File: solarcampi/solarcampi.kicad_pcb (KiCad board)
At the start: 2 copper layers, 65 x 30 mm, 6 parts, among them J1 Conn_02x20_Odd_Even

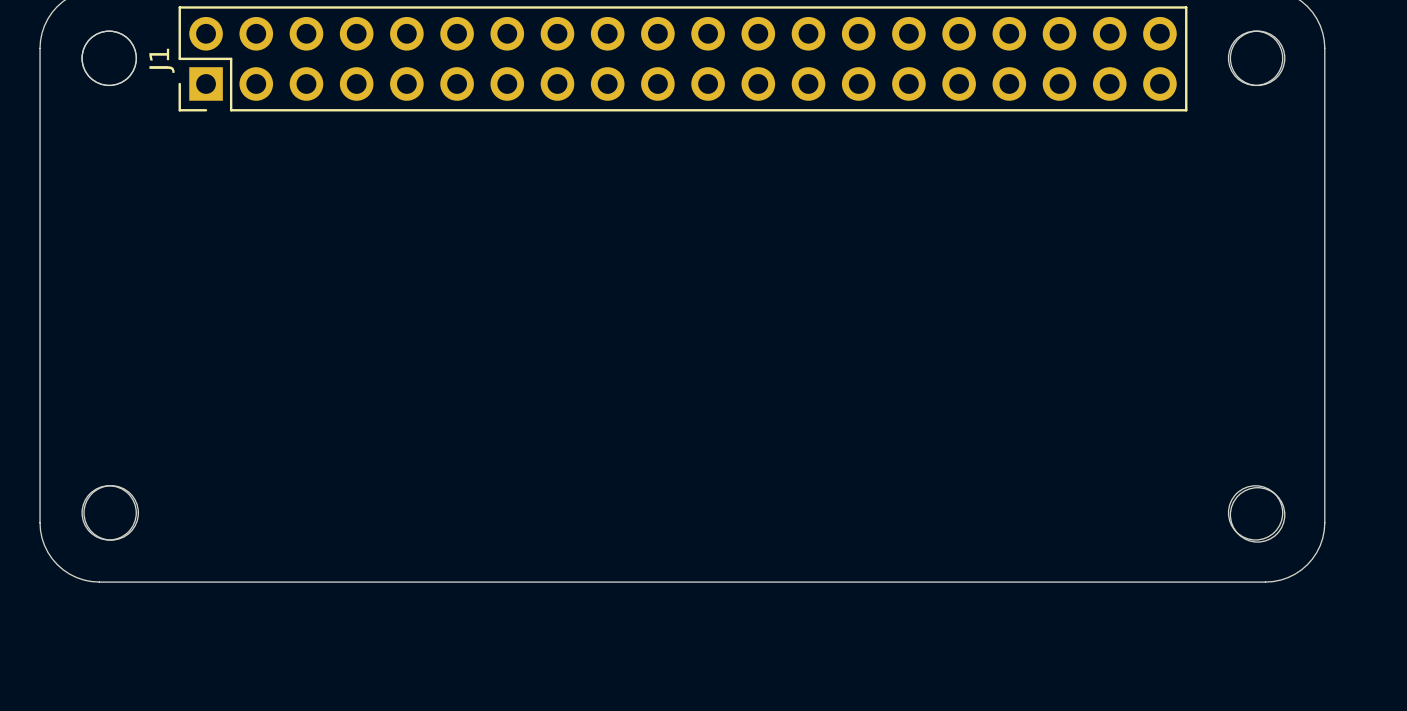
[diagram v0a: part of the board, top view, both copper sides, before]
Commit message: Add fuse, add decoupling caps, set footprints
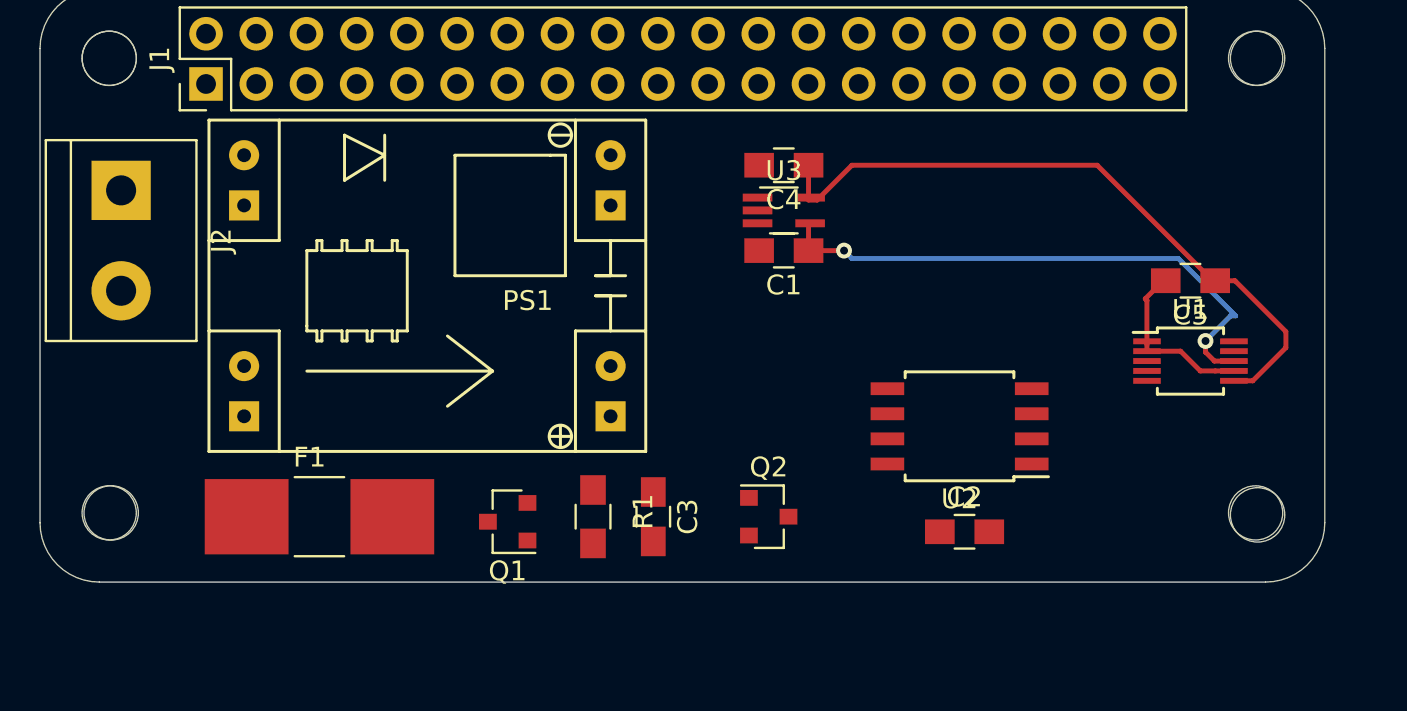
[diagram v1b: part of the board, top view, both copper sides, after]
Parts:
- added C1: 100n, Capacitors_SMD:C_0805_HandSoldering, F.Cu at (87.6, 62.2)
- added C2: 100n, Capacitors_SMD:C_0805_HandSoldering, F.Cu at (96.8, 76.5)
- added C3: 100n, Capacitors_SMD:C_0805_HandSoldering, F.Cu at (81.0, 75.7)
- added C4: 1µF, Capacitors_SMD:C_0805_HandSoldering, F.Cu at (87.6, 57.9)
- added C5: 100n, Capacitors_SMD:C_0805_HandSoldering, F.Cu at (108.2, 63.8)
- added F1: 1A, solarcampi:Fuse_SMD_HASF, F.Cu at (64.1, 75.7)
- added J2: Vin 12V, Connectors:bornier2, F.Cu at (54.1, 59.2)
- added PS1: MP1584EN, solarcampi:MP1584_buck_module, F.Cu at (69.6, 64.0)
- added Q1: IRLML 2244, TO_SOT_Packages_SMD:SOT-23, F.Cu at (73.7, 75.9)
- added Q2: BCR 108 SMD, TO_SOT_Packages_SMD:SOT-23, F.Cu at (86.9, 75.7)
- added R1: 10k, Resistors_SMD:R_0805_HandSoldering, F.Cu at (78.0, 75.7)
- added U1: INA226, Housings_SSOP:MSOP-10_3x3mm_Pitch0.5mm, F.Cu at (108.2, 67.8)
- added U2: ATtiny85-20SU, Housings_SOIC:SOIJ-8_5.3x5.3mm_Pitch1.27mm, F.Cu at (96.5, 71.1)
- added U3: TPS71533__SC70, TO_SOT_Packages_SMD:SOT-353_SC-70-5_Handsoldering, F.Cu at (87.6, 60.2)
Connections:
- J1 pad 6: Net-(J1-Pad6) -> GND
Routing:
- net +3V3: track 0.00 -> 34.3 mm
- net +12V: track 0.00 -> 28.6 mm, vias 0 -> 2
- net GND: track 0.00 -> 8.92 mm

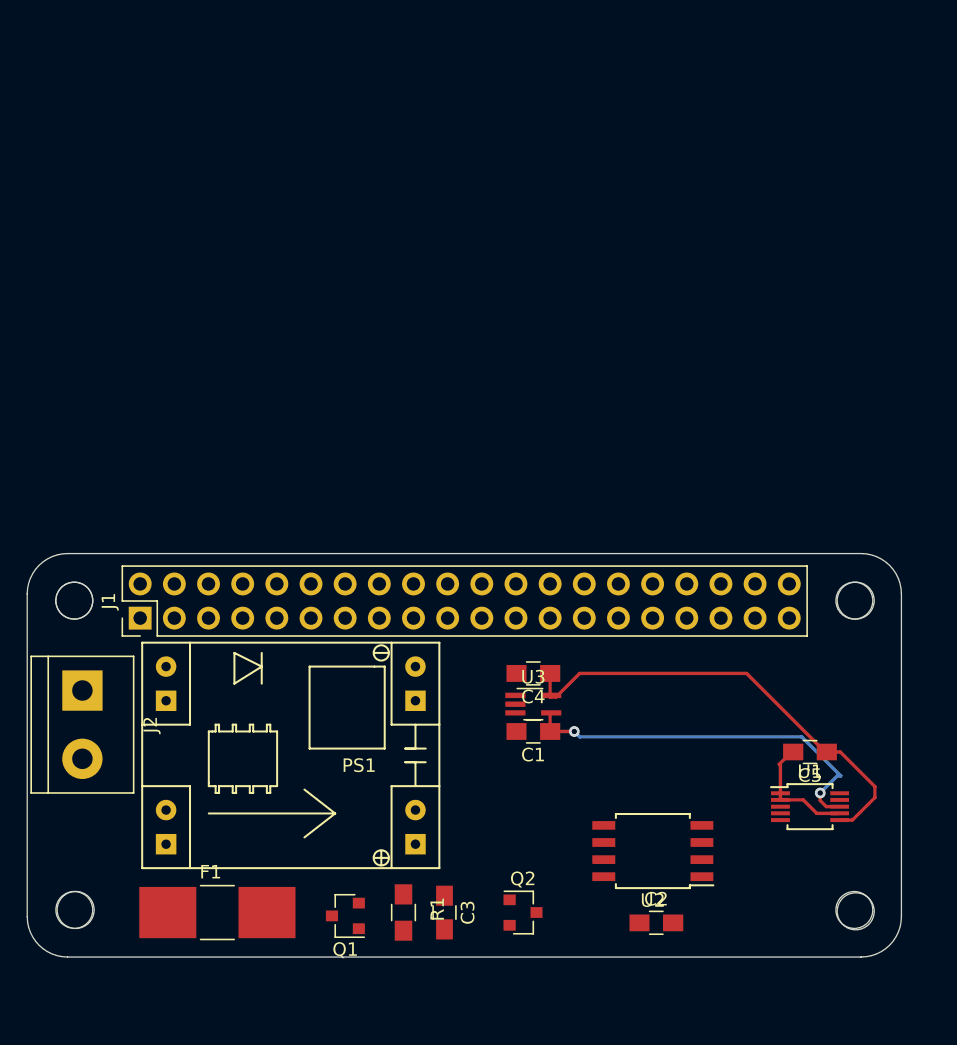
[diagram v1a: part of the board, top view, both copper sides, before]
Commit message: Add ISP header, FTDI header, more caps, power switching for INA and 2 I2C busses
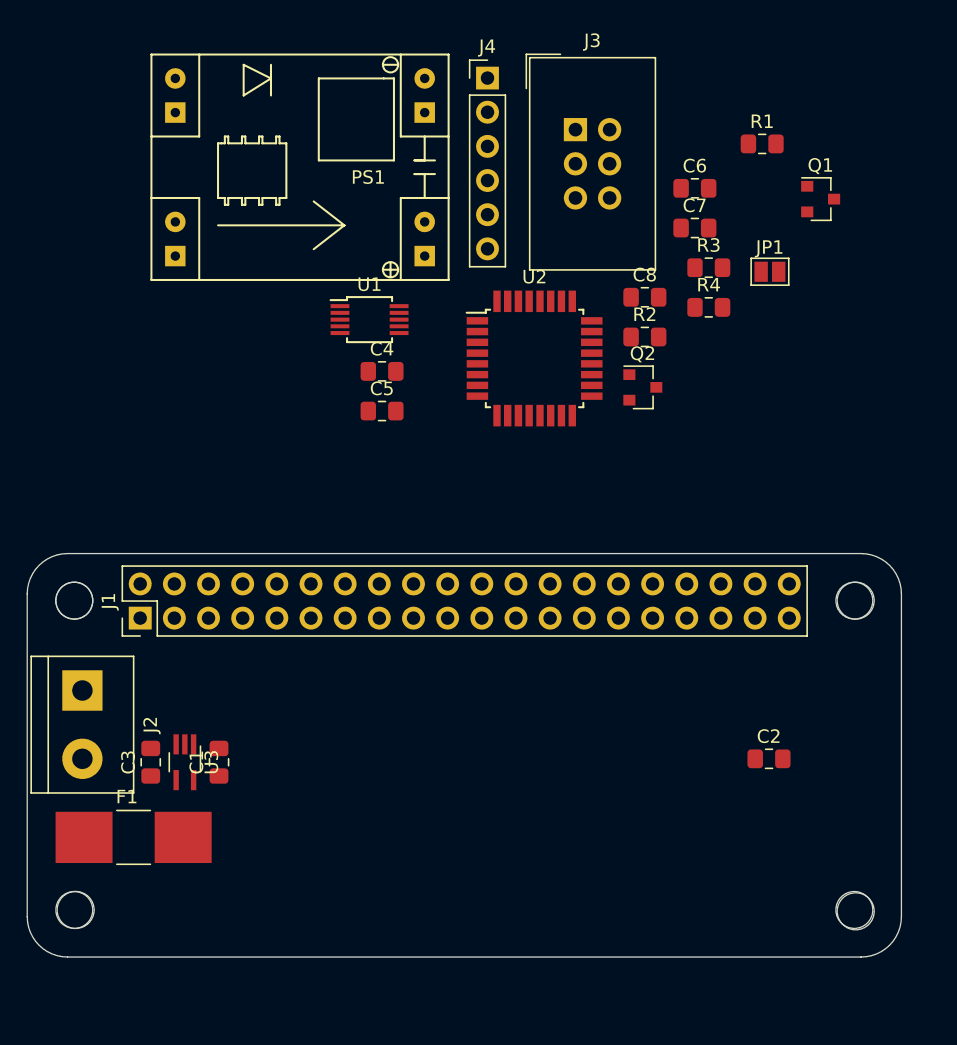
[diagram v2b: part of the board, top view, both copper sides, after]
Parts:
- added C6: 100n, Capacitor_SMD:C_0805_2012Metric_Pad1.15x1.40mm_HandSolder, F.Cu at (99.6, 21.8)
- added C7: 10µ, Capacitor_SMD:C_0805_2012Metric_Pad1.15x1.40mm_HandSolder, F.Cu at (99.6, 24.8)
- added C8: 10µ, Capacitor_SMD:C_0805_2012Metric_Pad1.15x1.40mm_HandSolder, F.Cu at (95.9, 29.9)
- added J3: AVR-ISP-6, Connector_IDC:IDC-Header_2x03_P2.54mm_Vertical, F.Cu at (90.8, 17.5)
- added J4: FTDI, Connector_PinHeader_2.54mm:PinHeader_1x06_P2.54mm_Vertical, F.Cu at (84.2, 13.6)
- added JP1: Jumper_2_Open, Jumper:SolderJumper-2_P1.3mm_Open_Pad1.0x1.5mm, F.Cu at (105.2, 28.0)
- added R2: 10k, Resistor_SMD:R_0805_2012Metric_Pad1.15x1.40mm_HandSolder, F.Cu at (95.9, 32.9)
- added R3: 4k7, Resistor_SMD:R_0805_2012Metric_Pad1.15x1.40mm_HandSolder, F.Cu at (100.7, 27.7)
- added R4: 4k7, Resistor_SMD:R_0805_2012Metric_Pad1.15x1.40mm_HandSolder, F.Cu at (100.7, 30.7)
- C1, C2, C3, C4, C5: footprint Capacitors_SMD:C_0805_HandSoldering -> Capacitor_SMD:C_0805_2012Metric_Pad1.15x1.40mm_HandSolder
- J2: footprint Connectors:bornier2 -> TerminalBlock:TerminalBlock_bornier-2_P5.08mm
- Q1, Q2: footprint TO_SOT_Packages_SMD:SOT-23 -> Package_TO_SOT_SMD:SOT-23
- R1: footprint Resistors_SMD:R_0805_HandSoldering -> Resistor_SMD:R_0805_2012Metric_Pad1.15x1.40mm_HandSolder
- U1: footprint Housings_SSOP:MSOP-10_3x3mm_Pitch0.5mm -> Package_SO:MSOP-10_3x3mm_P0.5mm
- U2: value ATtiny85-20SU -> ATmega328P-AU; footprint Housings_SOIC:SOIJ-8_5.3x5.3mm_Pitch1.27mm -> Package_QFP:TQFP-32_7x7mm_P0.8mm
- U3: footprint TO_SOT_Packages_SMD:SOT-353_SC-70-5_Handsoldering -> Package_TO_SOT_SMD:SOT-353_SC-70-5_Handsoldering
- moved Q1 63.9 mm to (109.0, 22.6), turned to 0 degrees
- moved R1 63.1 mm to (104.6, 18.5), turned to 0 degrees
- moved U1 48.8 mm to (75.5, 31.6)
- moved PS1 43.7 mm to (70.3, 20.3)
- moved C5 40.7 mm to (76.4, 38.4), turned to 0 degrees
- moved Q2 40.1 mm to (95.8, 36.6)
- moved U2 37.7 mm to (87.7, 34.5), turned to 0 degrees
- moved U3 26.3 mm to (61.7, 64.5), turned to 270 degrees
- moved C4 25.1 mm to (76.4, 35.5), turned to 0 degrees
- moved C3 24.5 mm to (59.2, 64.5), turned to 90 degrees
- moved C1 23.5 mm to (64.3, 64.5), turned to 90 degrees
- moved C2 14.8 mm to (105.2, 64.3)
- moved F1 8.37 mm to (57.9, 70.1)
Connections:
- C5 pad 1: +3V3 -> /INA_3V3
- J1 pad 10: Net-(J1-Pad10) -> /TX
- J1 pad 3: Net-(J1-Pad3) -> /RPI_SDA
- J1 pad 5: Net-(J1-Pad5) -> /RPI_SCL
- J1 pad 7: Net-(J1-Pad7) -> /RPI_SHDN
- J1 pad 8: Net-(J1-Pad8) -> /RX
- U1 pad 4: Net-(U1-Pad4) -> /AVR_SDA
- U1 pad 5: Net-(U1-Pad5) -> /AVR_SCL
- U1 pad 6: +3V3 -> /INA_3V3
- U2 pad 1: Net-(U2-Pad1) -> /AVR_SDA
- U2 pad 2: Net-(Q2-Pad1) -> /AVR_SCL
- U2 pad 3: Net-(J1-Pad7) -> GND
- U2 pad 4: GND -> +3V3
- U2 pad 5: Net-(U1-Pad4) -> GND
- U2 pad 6: Net-(U2-Pad6) -> +3V3
- U2 pad 7: Net-(U1-Pad5) -> Net-(U2-Pad7)
- U2 pad 8: +3V3 -> Net-(U2-Pad8)
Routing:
- net +3V3: track 34.3 -> 0.00 mm
- net +12V: track 28.6 -> 0.00 mm, vias 2 -> 0
- net GND: track 8.92 -> 0.00 mm
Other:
- net class Default: clearance 0.2 -> 0.127; via_dia 0.8 -> 0.6; via_drill 0.4 -> 0.3
- rule trace_clearance: 0.2 -> 0.127
- rule trace_min: 0.2 -> 0.127
- rule via_min_size: 0.4 -> 0.6

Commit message: Component placement v1
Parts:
- C1, C2, C5, C6, JP1, Q1, Q2, R2, U1, U2: moved to B.Cu
- moved R1 58.5 mm to (84.3, 73.4)
- moved J3 58.0 mm to (96.3, 75.2), turned to 90 degrees
- moved Q1 53.3 mm to (84.3, 69.8), turned to 90 degrees
- moved PS1 47.8 mm to (80.3, 67.1), turned to 90 degrees
- moved J4 46.9 mm to (68.8, 57.9)
- moved JP1 46.4 mm to (92.6, 72.6)
- moved R3 40.4 mm to (85.6, 65.3), turned to 270 degrees
- moved C7 37.6 mm to (96.3, 62.2), turned to 90 degrees
- moved R4 37.0 mm to (87.6, 65.3), turned to 270 degrees
- moved C6 36.8 mm to (103.4, 58.4), turned to 270 degrees
- moved Q2 35.0 mm to (88.4, 70.9), turned to 180 degrees
- moved C4 32.5 mm to (63.5, 65.3)
- moved C8 31.8 mm to (80.3, 57.7), turned to 180 degrees
- moved U1 31.5 mm to (85.3, 61.5), turned to 180 degrees
- moved U2 29.7 mm to (96.0, 63.0), turned to 180 degrees
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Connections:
- R3 pad 1: /AVR_SCL -> /AVR_SDA
- R4 pad 1: /AVR_SDA -> /AVR_SCL
- U2 pad 1: /AVR_SDA -> Net-(U2-Pad1)
- U2 pad 19: Net-(U2-Pad19) -> /AVR_I2C_PULLUP
- U2 pad 2: /AVR_SCL -> Net-(U2-Pad2)
- U2 pad 23: Net-(U2-Pad23) -> /AVR_SCL
- U2 pad 24: Net-(U2-Pad24) -> /AVR_SDA
- U2 pad 9: /AVR_I2C_PULLUP -> Net-(U2-Pad9)

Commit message: Route everything
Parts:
- added C9: 100n, Capacitor_SMD:C_0805_2012Metric_Pad1.15x1.40mm_HandSolder, F.Cu at (79.5, 65.7)
- moved R4 3.08 mm to (84.6, 65.7)
- moved R3 1.98 mm to (87.5, 65.7)
- moved C4 0.43 mm to (63.5, 64.8)
- moved U3 0.33 mm to (61.9, 61.4)
- moved C8 0.10 mm to (80.2, 57.8)
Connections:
- net +12VA renamed /+12V_SWITCHED
- net Net-(C8-Pad1) renamed /RPI_5V
- net Net-(Q2-Pad1) renamed /AVR_PWR_EN
- R3 pad 1: /AVR_SDA -> /AVR_SCL
- R4 pad 1: /AVR_SCL -> /AVR_SDA
- U2 pad 10: /INA_3V3 -> Net-(U2-Pad10)
- U2 pad 22: Net-(U2-Pad22) -> /AVR_SCL
- U2 pad 23: /AVR_SCL -> /AVR_SDA
- U2 pad 24: /AVR_SDA -> /INA_3V3
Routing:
- net +3V3: track 0.00 -> 67.0 mm, vias 0 -> 2
- net +12V: track 0.00 -> 63.7 mm, vias 0 -> 3
- net /RPI_SHDN: track 0.00 -> 43.1 mm
- net /RPI_SDA: track 0.00 -> 37.6 mm
- net /RPI_5V: track 0.00 -> 36.2 mm, vias 0 -> 1
- net /RPI_SCL: track 0.00 -> 36.0 mm
- net /~RST: track 0.00 -> 28.9 mm
- net /SCK: track 0.00 -> 19.3 mm
- net /RX: track 0.00 -> 18.0 mm
- net /TX: track 0.00 -> 15.9 mm
- net /INA_3V3: track 0.00 -> 14.3 mm
- net /AVR_I2C_PULLUP: track 0.00 -> 14.1 mm, vias 0 -> 1
- net /AVR_PWR_EN: track 0.00 -> 10.8 mm, vias 0 -> 2
- net Net-(J3-Pad2): track 0.00 -> 10.5 mm
- net /MISO: track 0.00 -> 10.0 mm
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- added copper zone on B.Cu, net GND
- added copper zone on F.Cu, net GND

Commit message: RevA finished
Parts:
- J2: footprint TerminalBlock:TerminalBlock_bornier-2_P5.08mm -> solarcampi:zweipolige_Anreihklemme
- renumbered J4 to FTDI, J1 to RPI, JP1 to TGT_PWR
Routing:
- net /INA_3V3: track 14.3 -> 15.7 mm
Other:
- board text added: "AVR ISP"
- board text added: "SolarCamPi RevA"
- board text added: "Tobias Mädel Tobias Schramm"
